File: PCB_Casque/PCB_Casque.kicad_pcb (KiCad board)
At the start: 2 copper layers, 80 x 80 mm, 41 parts, among them J1 USB_C_Receptacle_USB2.0_16P, J2 Conn_01x02_Pin, J3 Conn_01x01_Pin, J4 Conn_01x01_Pin, J5 Conn_01x01_Pin, J6 Conn_01x01_Pin, SW1 SW_Push, SW2 SW_Push, SW3 SW_Push, SW4 SW_Push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

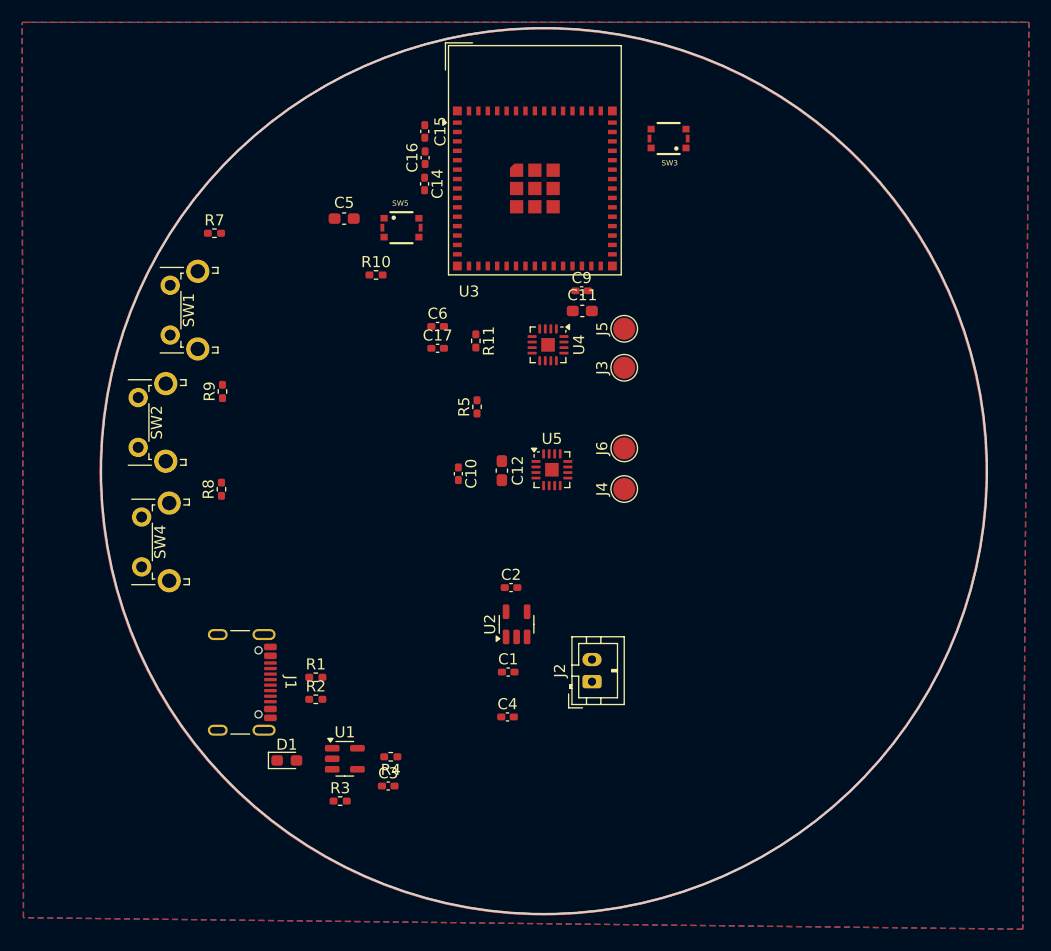
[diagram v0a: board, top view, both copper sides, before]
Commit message: ajout du PCB version final + elt du design
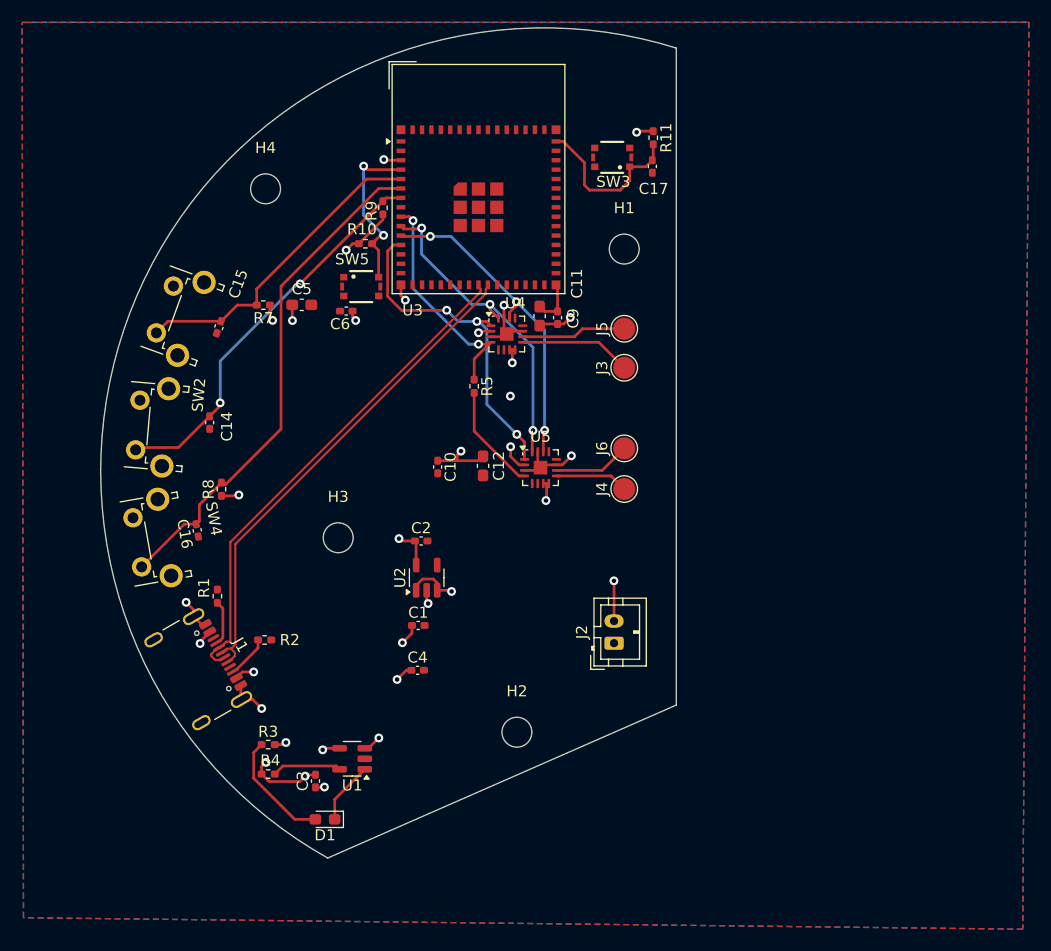
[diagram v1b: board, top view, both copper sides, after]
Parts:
- added H1: MountingHole, MountingHole:MountingHole_2.7mm_M2.5, F.Cu at (146.3, 69.5)
- added H2: MountingHole, MountingHole:MountingHole_2.7mm_M2.5, F.Cu at (136.6, 113.1)
- added H3: MountingHole, MountingHole:MountingHole_2.7mm_M2.5, F.Cu at (120.5, 95.5)
- added H4: MountingHole, MountingHole:MountingHole_2.7mm_M2.5, F.Cu at (113.9, 64.0)
- moved C16 39.4 mm to (107.8, 94.9), turned to 100 degrees
- moved C14 29.0 mm to (108.9, 85.1), turned to 90 degrees
- moved C15 25.7 mm to (109.7, 76.5), turned to 70 degrees
- moved C17 25.4 mm to (148.8, 62.0), turned to 90 degrees
- moved R11 24.4 mm to (148.9, 59.4)
- moved R9 22.0 mm to (124.5, 65.7)
- moved R1 11.5 mm to (109.6, 100.8), turned to 90 degrees
- moved R4 11.2 mm to (114.2, 116.9)
- moved C1 9.15 mm to (127.7, 103.5)
- moved C2 9.15 mm to (128.0, 95.8)
- moved C4 9.15 mm to (127.7, 107.5)
- moved U2 9.15 mm to (128.5, 99.1)
- moved C5 8.68 mm to (117.2, 74.5)
- moved C6 8.37 mm to (121.2, 75.1)
- moved R3 8.26 mm to (114.2, 114.2)
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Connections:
- net /ESP23_s3_mini_1_N8/D+ renamed /ESP23_s3_mini_1_N8/DP
- net /ESP23_s3_mini_1_N8/D- renamed /ESP23_s3_mini_1_N8/DN
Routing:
- net /ESP23_s3_mini_1_N8/IO1: track 0.00 -> 46.2 mm
- net /ESP23_s3_mini_1_N8/DP: track 0.00 -> 45.2 mm
- net /ESP23_s3_mini_1_N8/DN: track 0.00 -> 45.0 mm
- net /ESP23_s3_mini_1_N8/IO2: track 0.00 -> 35.7 mm, vias 0 -> 2
- net GND: track 0.00 -> 32.2 mm, vias 0 -> 9
- net /DAC ampli droit/DIN: track 0.00 -> 30.4 mm, vias 0 -> 3
- net /DAC ampli droit/LRCLK: track 0.00 -> 29.4 mm, vias 0 -> 3
- net /Abaisseur/Vbat(3.7V): track 0.00 -> 29.3 mm, vias 0 -> 11
- net /DAC ampli droit/BCLK: track 0.00 -> 28.9 mm, vias 0 -> 3
- net /ESP23_s3_mini_1_N8/IO0: track 0.00 -> 28.7 mm
- net /DAC ampli droit/SD_Mode_droit: track 0.00 -> 20.5 mm, vias 0 -> 2
- net /ESP23_s3_mini_1_N8/Valim(3.3V): track 0.00 -> 17.3 mm, vias 0 -> 8
- net Net-(U3-IO0): track 0.00 -> 15.1 mm, vias 0 -> 2
- net EN: track 0.00 -> 15.0 mm
- net Net-(D1-A): track 0.00 -> 10.4 mm
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- added copper zone on In1.Cu, net /Abaisseur/V_USB(5V)
- added copper zone on In1.Cu, net /Abaisseur/Vbat(3.7V)
- added copper zone on In1.Cu, net /ESP23_s3_mini_1_N8/Valim(3.3V)
- added copper zone on In2.Cu, net GND
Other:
- board size 80 x 80 mm -> 52 x 75 mm
- copper layers 2 -> 4
